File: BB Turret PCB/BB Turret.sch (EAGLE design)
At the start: 7 parts, among them M1 SERVO, M2 SERVO

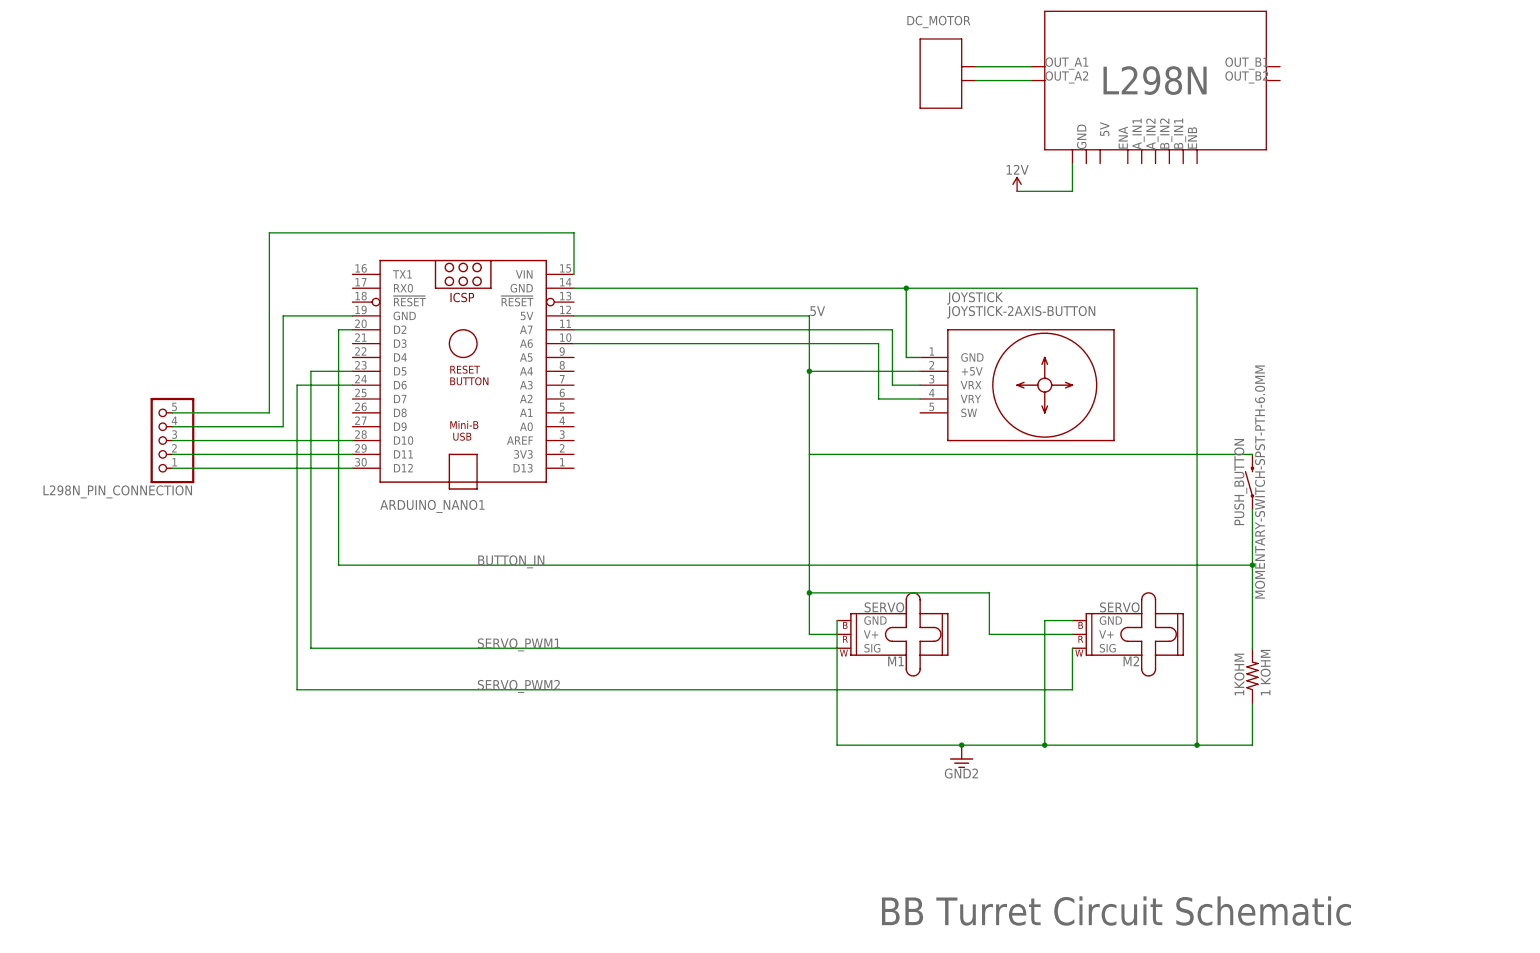
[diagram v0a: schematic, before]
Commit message: Updated PCB files to be up to date with the code and current breadboard circuit. Updated images and README.
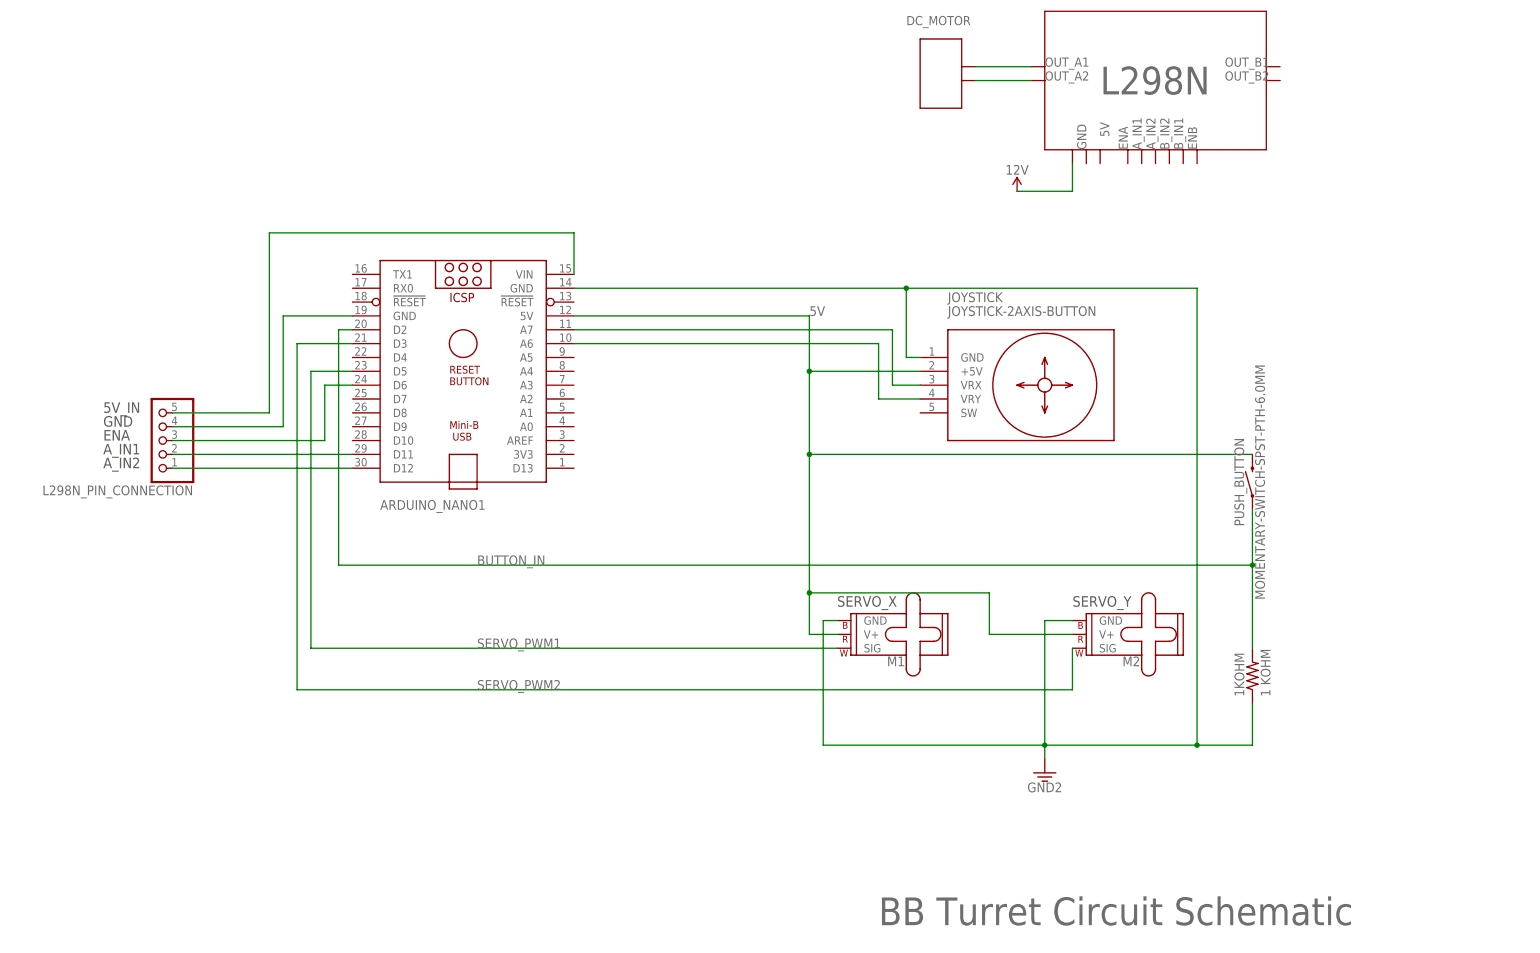
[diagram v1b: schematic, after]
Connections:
- net N$2 renamed A_IN2
- net N$3 renamed A_IN1
- net N$5 renamed 5V_IN
- removed net N$4: ARDUINO_NANO1.D10, L298N_PIN_CONNECTION.3
- new net ENA: ARDUINO_NANO1.D6, L298N_PIN_CONNECTION.3
- net SERVO_PWM2: now also ARDUINO_NANO1.D3; no longer ARDUINO_NANO1.D6
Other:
- note added: "5V_IN"
- note added: "SERVO_X"
- note added: "SERVO_Y"
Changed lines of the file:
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@@
 <wire x1="190.5" y1="180.34" x2="193.04" y2="180.34" width="0.1524" layer="94"/>
 <text x="180.34" y="190.5" size="1.6764" layer="95">DC_MOTOR</text>
+<text x="33.02" y="116.84" size="1.9304" layer="97">GND</text>
+<text x="33.02" y="119.38" size="1.9304" layer="97">5V_IN</text>
+<text x="167.64" y="83.82" size="1.9304" layer="97">SERVO_X</text>
+<text x="210.82" y="83.82" size="1.9304" layer="97">SERVO_Y</text>
+<text x="33.02" y="114.3" size="1.9304" layer="97">ENA</text>
+<text x="33.02" y="111.76" size="1.9304" layer="97">A_IN1</text>
+<text x="33.02" y="109.22" size="1.9304" layer="97">A_IN2</text>
 </plain>
 <instances>
@@
 <instance part="M1" gate="G$1" x="170.18" y="76.2" smashed="yes" rot="R180">
 <attribute name="NAME" x="180.086" y="74.676" size="1.778" layer="95" font="vector" rot="R180"/>
-<attribute name="VALUE" x="180.086" y="82.804" size="1.778" layer="95" font="vector" rot="R180" align="top-left"/>
 </instance>
 <instance part="M2" gate="G$1" x="213.36" y="76.2" smashed="yes" rot="R180">
 <attribute name="NAME" x="223.266" y="74.676" size="1.778" layer="95" font="vector" rot="R180"/>
-<attribute name="VALUE" x="223.266" y="82.804" size="1.778" layer="95" font="vector" rot="R180" align="top-left"/>
-</instance>
-<instance part="GND2" gate="G$1" x="190.5" y="55.88" smashed="yes">
-<attribute name="VALUE" x="190.5" y="54.102" size="1.778" layer="96" align="top-center"/>
+</instance>
+<instance part="GND2" gate="G$1" x="205.74" y="53.34" smashed="yes">
+<attribute name="VALUE" x="205.74" y="51.562" size="1.778" layer="96" align="top-center"/>
 </instance>
 <instance part="SUPPLY1" gate="G$1" x="200.66" y="160.02" smashed="yes">
@@
 </busses>
 <nets>
-<net name="COLLECTOR" class="0">
+<net name="OUT_A1" class="0">
 <segment>
 <wire x1="193.04" y1="182.88" x2="203.2" y2="182.88" width="0.1524" layer="91"/>
@@
 <segment>
 <wire x1="210.82" y1="68.58" x2="68.58" y2="68.58" width="0.1524" layer="91"/>
-<pinref part="ARDUINO_NANO1" gate="G$1" pin="D6"/>
-<wire x1="68.58" y1="68.58" x2="68.58" y2="124.46" width="0.1524" layer="91"/>
-<wire x1="68.58" y1="124.46" x2="78.74" y2="124.46" width="0.1524" layer="91"/>
+<wire x1="68.58" y1="68.58" x2="68.58" y2="132.08" width="0.1524" layer="91"/>
 <pinref part="M2" gate="G$1" pin="SIG"/>
 <wire x1="210.82" y1="68.58" x2="210.82" y2="76.2" width="0.1524" layer="91"/>
 <label x="101.6" y="68.58" size="1.778" layer="95"/>
+<pinref part="ARDUINO_NANO1" gate="G$1" pin="D3"/>
+<wire x1="68.58" y1="132.08" x2="78.74" y2="132.08" width="0.1524" layer="91"/>
 </segment>
 </net>
@@
 <wire x1="162.56" y1="137.16" x2="162.56" y2="127" width="0.1524" layer="91"/>
 <junction x="162.56" y="127"/>
+<junction x="162.56" y="111.76"/>
 </segment>
 </net>
 <net name="GND" class="0">
+<segment>
+<pinref part="ARDUINO_NANO1" gate="G$1" pin="GND@1"/>
+<wire x1="66.04" y1="137.16" x2="78.74" y2="137.16" width="0.1524" layer="91"/>
+<wire x1="66.04" y1="116.84" x2="66.04" y2="137.16" width="0.1524" layer="91"/>
+<pinref part="L298N_PIN_CONNECTION" gate="A" pin="4"/>
+<wire x1="45.72" y1="116.84" x2="66.04" y2="116.84" width="0.1524" layer="91"/>
+</segment>
 <segment>
 <pinref part="JOYSTICK" gate="G$1" pin="GND"/>
@@
 <wire x1="210.82" y1="81.28" x2="205.74" y2="81.28" width="0.1524" layer="91"/>
 <wire x1="205.74" y1="81.28" x2="205.74" y2="58.42" width="0.1524" layer="91"/>
-<junction x="205.74" y="58.42"/>
-<pinref part="M1" gate="G$1" pin="GND"/>
-<wire x1="167.64" y1="81.28" x2="167.64" y2="58.42" width="0.1524" layer="91"/>
-<wire x1="167.64" y1="58.42" x2="190.5" y2="58.42" width="0.1524" layer="91"/>
-<wire x1="190.5" y1="58.42" x2="205.74" y2="58.42" width="0.1524" layer="91"/>
-<pinref part="GND2" gate="G$1" pin="3.3V"/>
-<junction x="190.5" y="58.42"/>
 <pinref part="ARDUINO_NANO1" gate="G$1" pin="GND@2"/>
 <wire x1="119.38" y1="142.24" x2="180.34" y2="142.24" width="0.1524" layer="91"/>
 <junction x="180.34" y="142.24"/>
-</segment>
-<segment>
-<pinref part="ARDUINO_NANO1" gate="G$1" pin="GND@1"/>
-<wire x1="66.04" y1="137.16" x2="78.74" y2="137.16" width="0.1524" layer="91"/>
-<wire x1="66.04" y1="116.84" x2="66.04" y2="137.16" width="0.1524" layer="91"/>
-<pinref part="L298N_PIN_CONNECTION" gate="A" pin="4"/>
-<wire x1="45.72" y1="116.84" x2="66.04" y2="116.84" width="0.1524" layer="91"/>
-</segment>
-</net>
-<net name="N$1" class="0">
+<pinref part="M1" gate="G$1" pin="GND"/>
+<wire x1="167.64" y1="81.28" x2="165.1" y2="81.28" width="0.1524" layer="91"/>
+<wire x1="165.1" y1="81.28" x2="165.1" y2="58.42" width="0.1524" layer="91"/>
+<wire x1="165.1" y1="58.42" x2="205.74" y2="58.42" width="0.1524" layer="91"/>
+<junction x="205.74" y="58.42"/>
+<pinref part="GND2" gate="G$1" pin="3.3V"/>
+<wire x1="205.74" y1="58.42" x2="205.74" y2="55.88" width="0.1524" layer="91"/>
+</segment>
+</net>
+<net name="OUT_A2" class="0">
 <segment>
 <wire x1="193.04" y1="180.34" x2="203.2" y2="180.34" width="0.1524" layer="91"/>
@@
 </segment>
 </net>
-<net name="N$2" class="0">
+<net name="A_IN2" class="0">
 <segment>
 <pinref part="L298N_PIN_CONNECTION" gate="A" pin="1"/>
@@
 </segment>
 </net>
-<net name="N$3" class="0">
+<net name="A_IN1" class="0">
 <segment>
 <pinref part="L298N_PIN_CONNECTION" gate="A" pin="2"/>
@@
 </segment>
 </net>
-<net name="N$4" class="0">
-<segment>
-<pinref part="L298N_PIN_CONNECTION" gate="A" pin="3"/>
-<pinref part="ARDUINO_NANO1" gate="G$1" pin="D10"/>
-<wire x1="45.72" y1="114.3" x2="78.74" y2="114.3" width="0.1524" layer="91"/>
-</segment>
-</net>
-<net name="N$5" class="0">
+<net name="5V_IN" class="0">
 <segment>
 <pinref part="ARDUINO_NANO1" gate="G$1" pin="VIN"/>
@@
 </segment>
 </net>
+<net name="ENA" class="0">
+<segment>
+<pinref part="L298N_PIN_CONNECTION" gate="A" pin="3"/>
+<wire x1="45.72" y1="114.3" x2="73.66" y2="114.3" width="0.1524" layer="91"/>
+<wire x1="73.66" y1="114.3" x2="73.66" y2="124.46" width="0.1524" layer="91"/>
+<pinref part="ARDUINO_NANO1" gate="G$1" pin="D6"/>
+<wire x1="73.66" y1="124.46" x2="78.74" y2="124.46" width="0.1524" layer="91"/>
+</segment>
+</net>
 </nets>
 </sheet>
 </sheets>
+<errors>
+</errors>
 </schematic>
 </drawing>

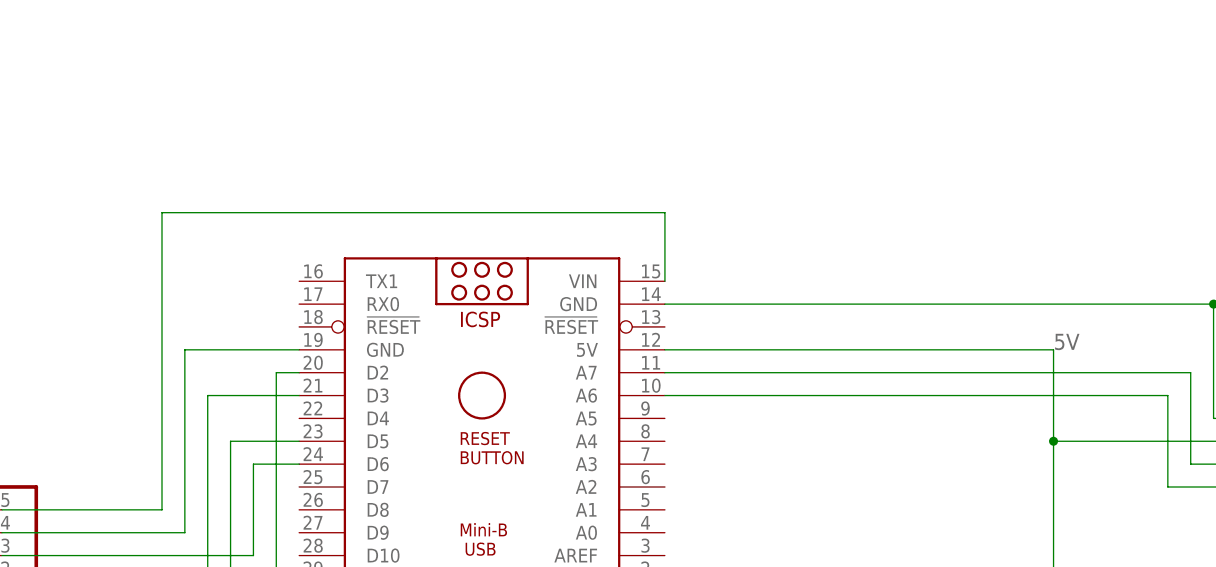
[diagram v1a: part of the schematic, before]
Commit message: Fixed circuit and PCB so that the Arduino does not need USB power.
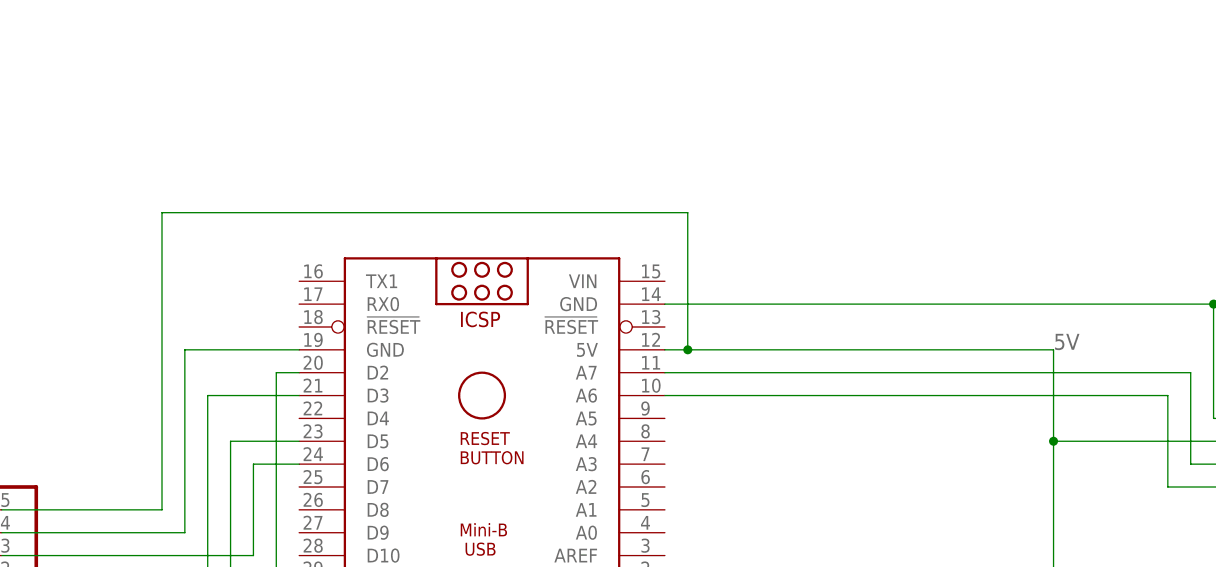
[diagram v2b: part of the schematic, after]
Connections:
- removed net 5V_IN: ARDUINO_NANO1.VIN, L298N_PIN_CONNECTION.5
- net 5V: now also L298N_PIN_CONNECTION.5
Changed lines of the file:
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@@
-</segment>
-</net>
-<net name="5V" class="0">
-<segment>
-<pinref part="JOYSTICK" gate="G$1" pin="+5V"/>
-<wire x1="162.56" y1="127" x2="182.88" y2="127" width="0.1524" layer="91"/>
-<wire x1="162.56" y1="127" x2="162.56" y2="111.76" width="0.1524" layer="91"/>
-<wire x1="162.56" y1="111.76" x2="162.56" y2="86.36" width="0.1524" layer="91"/>
-<wire x1="162.56" y1="86.36" x2="162.56" y2="78.74" width="0.1524" layer="91"/>
-<wire x1="162.56" y1="111.76" x2="243.84" y2="111.76" width="0.1524" layer="91"/>
-<pinref part="PUSH_BUTTON" gate="G$1" pin="2"/>
-<pinref part="M1" gate="G$1" pin="V+"/>
-<wire x1="167.64" y1="78.74" x2="162.56" y2="78.74" width="0.1524" layer="91"/>
-<pinref part="M2" gate="G$1" pin="V+"/>
-<wire x1="210.82" y1="78.74" x2="195.58" y2="78.74" width="0.1524" layer="91"/>
-<wire x1="195.58" y1="78.74" x2="195.58" y2="86.36" width="0.1524" layer="91"/>
-<wire x1="195.58" y1="86.36" x2="162.56" y2="86.36" width="0.1524" layer="91"/>
-<junction x="162.56" y="86.36"/>
-<label x="162.56" y="137.16" size="1.778" layer="95"/>
-<pinref part="ARDUINO_NANO1" gate="G$1" pin="5V"/>
-<wire x1="119.38" y1="137.16" x2="162.56" y2="137.16" width="0.1524" layer="91"/>
-<wire x1="162.56" y1="137.16" x2="162.56" y2="127" width="0.1524" layer="91"/>
-<junction x="162.56" y="127"/>
-<junction x="162.56" y="111.76"/>
 </segment>
 </net>
@@
 </segment>
 </net>
-<net name="5V_IN" class="0">
-<segment>
-<pinref part="ARDUINO_NANO1" gate="G$1" pin="VIN"/>
-<pinref part="L298N_PIN_CONNECTION" gate="A" pin="5"/>
-<wire x1="45.72" y1="119.38" x2="63.5" y2="119.38" width="0.1524" layer="91"/>
-<wire x1="63.5" y1="119.38" x2="63.5" y2="152.4" width="0.1524" layer="91"/>
-<wire x1="63.5" y1="152.4" x2="119.38" y2="152.4" width="0.1524" layer="91"/>
-<wire x1="119.38" y1="152.4" x2="119.38" y2="144.78" width="0.1524" layer="91"/>
-</segment>
-</net>
 <net name="ENA" class="0">
 <segment>
@@
 </segment>
 </net>
+<net name="5V" class="0">
+<segment>
+<pinref part="L298N_PIN_CONNECTION" gate="A" pin="5"/>
+<wire x1="45.72" y1="119.38" x2="63.5" y2="119.38" width="0.1524" layer="91"/>
+<wire x1="63.5" y1="119.38" x2="63.5" y2="152.4" width="0.1524" layer="91"/>
+<wire x1="63.5" y1="152.4" x2="121.92" y2="152.4" width="0.1524" layer="91"/>
+<pinref part="JOYSTICK" gate="G$1" pin="+5V"/>
+<wire x1="162.56" y1="127" x2="182.88" y2="127" width="0.1524" layer="91"/>
+<wire x1="162.56" y1="127" x2="162.56" y2="111.76" width="0.1524" layer="91"/>
+<wire x1="162.56" y1="111.76" x2="162.56" y2="86.36" width="0.1524" layer="91"/>
+<wire x1="162.56" y1="86.36" x2="162.56" y2="78.74" width="0.1524" layer="91"/>
+<wire x1="162.56" y1="111.76" x2="243.84" y2="111.76" width="0.1524" layer="91"/>
+<pinref part="PUSH_BUTTON" gate="G$1" pin="2"/>
+<pinref part="M1" gate="G$1" pin="V+"/>
+<wire x1="167.64" y1="78.74" x2="162.56" y2="78.74" width="0.1524" layer="91"/>
+<pinref part="M2" gate="G$1" pin="V+"/>
+<wire x1="210.82" y1="78.74" x2="195.58" y2="78.74" width="0.1524" layer="91"/>
+<wire x1="195.58" y1="78.74" x2="195.58" y2="86.36" width="0.1524" layer="91"/>
+<wire x1="195.58" y1="86.36" x2="162.56" y2="86.36" width="0.1524" layer="91"/>
+<junction x="162.56" y="86.36"/>
+<label x="162.56" y="137.16" size="1.778" layer="95"/>
+<pinref part="ARDUINO_NANO1" gate="G$1" pin="5V"/>
+<wire x1="119.38" y1="137.16" x2="121.92" y2="137.16" width="0.1524" layer="91"/>
+<wire x1="121.92" y1="137.16" x2="162.56" y2="137.16" width="0.1524" layer="91"/>
+<wire x1="162.56" y1="137.16" x2="162.56" y2="127" width="0.1524" layer="91"/>
+<junction x="162.56" y="127"/>
+<junction x="162.56" y="111.76"/>
+<wire x1="121.92" y1="152.4" x2="121.92" y2="137.16" width="0.1524" layer="91"/>
+<junction x="121.92" y="137.16"/>
+</segment>
+</net>
